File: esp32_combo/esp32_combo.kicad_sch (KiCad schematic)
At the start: 33 parts, among them J1 TERM BLK 3.5MM 2P SIDE, J2 TERM BLK 3.5MM 6P SIDE, J3 TERM BLK 3.5MM 6P SIDE, J4 TERM BLK 3.5MM 3P SIDE, J5 TERM BLK 3.5MM 3P SIDE, J6 HDR SKT 5PIN VERT 2.54MM, J7 HDR SKT 6PIN VERT 2.54MM, J8 SKT 2x6PIN VERT 2.54MM, J9 HDR SKT 8PIN VERT 2.54MM, Q1 AS2302, SW1 SS12D10, U1 TB6612FNG Module, U2 ESP32 DEV KIT Module 30-pin, U3 LM2596 Module

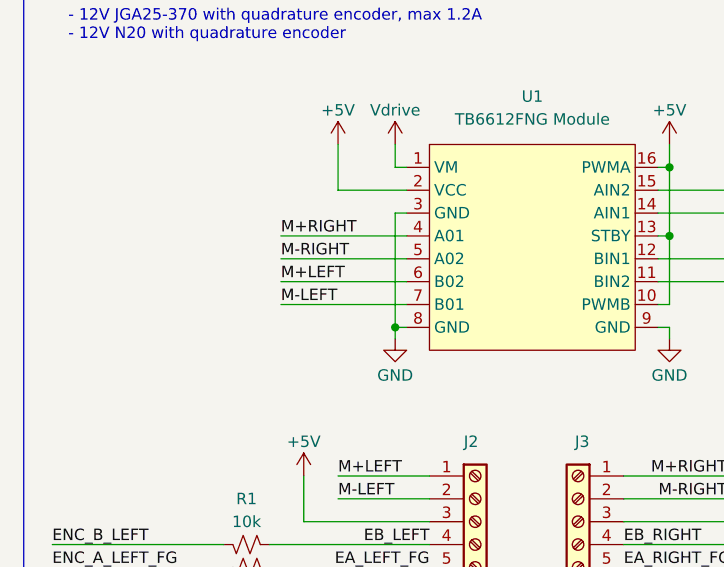
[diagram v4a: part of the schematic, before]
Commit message: Motor direction bugfix
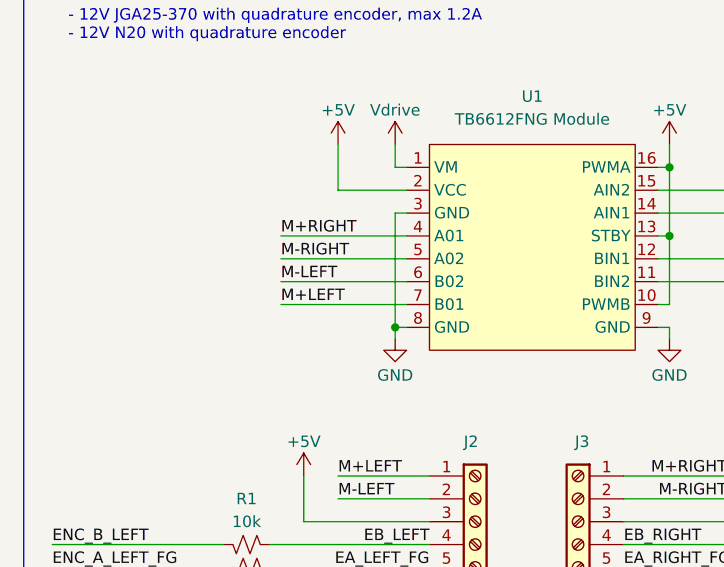
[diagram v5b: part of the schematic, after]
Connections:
- net M+LEFT: now also U1.7 (B01); no longer U1.6 (B02)
- net M-LEFT: now also U1.6 (B02); no longer U1.7 (B01)
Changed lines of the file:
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@@
-		)
-	)
-	(label "M+LEFT"
-		(at 43.18 110.49 0)
-		(fields_autoplaced yes)
-		(effects
-			(font
-				(size 1.27 1.27)
-			)
-			(justify left bottom)
 		)
 	)
@@
 		)
 	)
-	(label "M-LEFT"
-		(at 43.18 113.03 0)
-		(fields_autoplaced yes)
-		(effects
-			(font
-				(size 1.27 1.27)
-			)
-			(justify left bottom)
-		)
-	)
 	(label "LDS_RX"
 		(at 250.19 128.27 180)
@@
 		)
 	)
+	(label "M+LEFT"
+		(at 43.18 113.03 0)
+		(fields_autoplaced yes)
+		(effects
+			(font
+				(size 1.27 1.27)
+			)
+			(justify left bottom)
+		)
+	)
 	(label "GPIO39_IN"
 		(at 13.97 29.21 0)
@@
 		)
 	)
+	(label "M-LEFT"
+		(at 43.18 110.49 0)
+		(fields_autoplaced yes)
+		(effects
+			(font
+				(size 1.27 1.27)
+			)
+			(justify left bottom)
+		)
+	)

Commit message: Combo routed
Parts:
- removed J7: HDR SKT 6PIN VERT 2.54MM, Connector_PinSocket_2.54mm:PinSocket_1x06_P2.54mm_Vertical, symbol Connector_Generic:Conn_01x06
- removed J8: SKT 2x6PIN VERT 2.54MM, Connector_PinSocket_2.54mm:PinSocket_2x06_P2.54mm_Vertical, symbol Makerspet:Conn_02x06_Odd_Even_Key2
- removed J9: HDR SKT 8PIN VERT 2.54MM, Connector_PinSocket_2.54mm:PinSocket_1x08_P2.54mm_Vertical, symbol Makerspet:Conn_01x08_Key2
- added J7: HDR SKT 5PIN VERT 2.54MM, Connector_PinSocket_2.54mm:PinSocket_1x05_P2.54mm_Vertical, symbol Connector_Generic:Conn_01x05
- added J8: SKT 2x5PIN VERT 2.54MM, Connector_PinSocket_2.54mm:PinSocket_2x05_P2.54mm_Vertical, symbol Connector_Generic:Conn_02x05_Odd_Even
- added J9: HDR SKT 7PIN VERT 2.54MM, Connector_PinSocket_2.54mm:PinSocket_1x07_P2.54mm_Vertical, symbol Connector_Generic:Conn_01x07
- J6: symbol Makerspet:Conn_01x05_Key2 -> Connector_Generic:Conn_01x05
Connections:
- net +5V: now also J8.10 (Pin_10), J8.9 (Pin_9), J9.2 (Pin_2)
- net CW_RIGHT: now also U2.28 (RTC_GPIO14/HSPI_MOSI/TOUCH4/ADC2_CH4/GPIO13); no longer U2.23 (RTC_GPIO6/DAC1/ADC2_CH8/GPIO25)
- net GND: now also J7.1 (Pin_1), J8.1 (Pin_1), J8.2 (Pin_2), J9.1 (Pin_1)
- net GPIO18: now also J7.3 (Pin_3)
- net GPIO27: now also J7.2 (Pin_2)
- net GPIO4: now also J7.5 (Pin_5)
- net GPIO5_BOOT_STRAP: now also J7.4 (Pin_4)
- net I2C_INT: now also J8.7 (Pin_7), J8.8 (Pin_8)
- net I2C_SCL: now also J8.3 (Pin_3), J8.4 (Pin_4)
- net I2C_SDA: now also J8.5 (Pin_5), J8.6 (Pin_6)
- net LDS_EN: now also J9.7 (Pin_7)
- net LDS_PWM: now also J9.3 (Pin_3)
- net LDS_RX: now also J9.5 (Pin_5)
- net MOT: now also J9.6 (Pin_6)
- net PWM_RIGHT: now also U2.23 (RTC_GPIO6/DAC1/ADC2_CH8/GPIO25); no longer U2.28 (RTC_GPIO14/HSPI_MOSI/TOUCH4/ADC2_CH4/GPIO13)
- net at R11.2: now also J9.4 (Pin_4)
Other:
- note added: "BATTERY"
- note added: "GND GND Echo/Rx Trig/Tx VCC 5V"
- note added: "MOTORS - BRUSHLESS !! REMOVE TB6612FNG if using 24V (>12V) motors !! Up to 24V, ~1.3A max total per motor - CHR-GM25-BL2418 12V 225RPM 120PPR 0.65W - CHR-GM25-BL2418 24V 200RPM 270PPR 2.5W - JGA25-BL2418 24V 245RPM 630PPR - CHR-GM25-BL2418 24V 260RPM 204PPR 2.5W - JGA25-BL2418 24V 408RPM 127.8PPR - CHR-GM25-BL2418 24V 450RPM 120PPR 2.5W"
- note added: "NOTE: CW_RIGHT, PWM_RIGHT have been swapped"
- note removed: "BATTERY 12V"
- note removed: "MOTORS - BRUSHLESS - CHR-GM25-BLDC2418 i45 12V, 5V I/O"
- note removed: "VCC 5V Trig/Tx Echo/Rx GND GND"
- title: ESP32 Combo -> MakersCombo
- moved on the sheet: J4, J5, R10, R8, R9
